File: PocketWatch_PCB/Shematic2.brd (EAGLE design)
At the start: 45 x 25 mm, 53 parts, among them IC1 74HC139D, Q1 BCX71SMD, Q2 BCX71SMD, Q3 BCX71SMD, Q4 BCX71SMD, U2 ATTINY88-AU

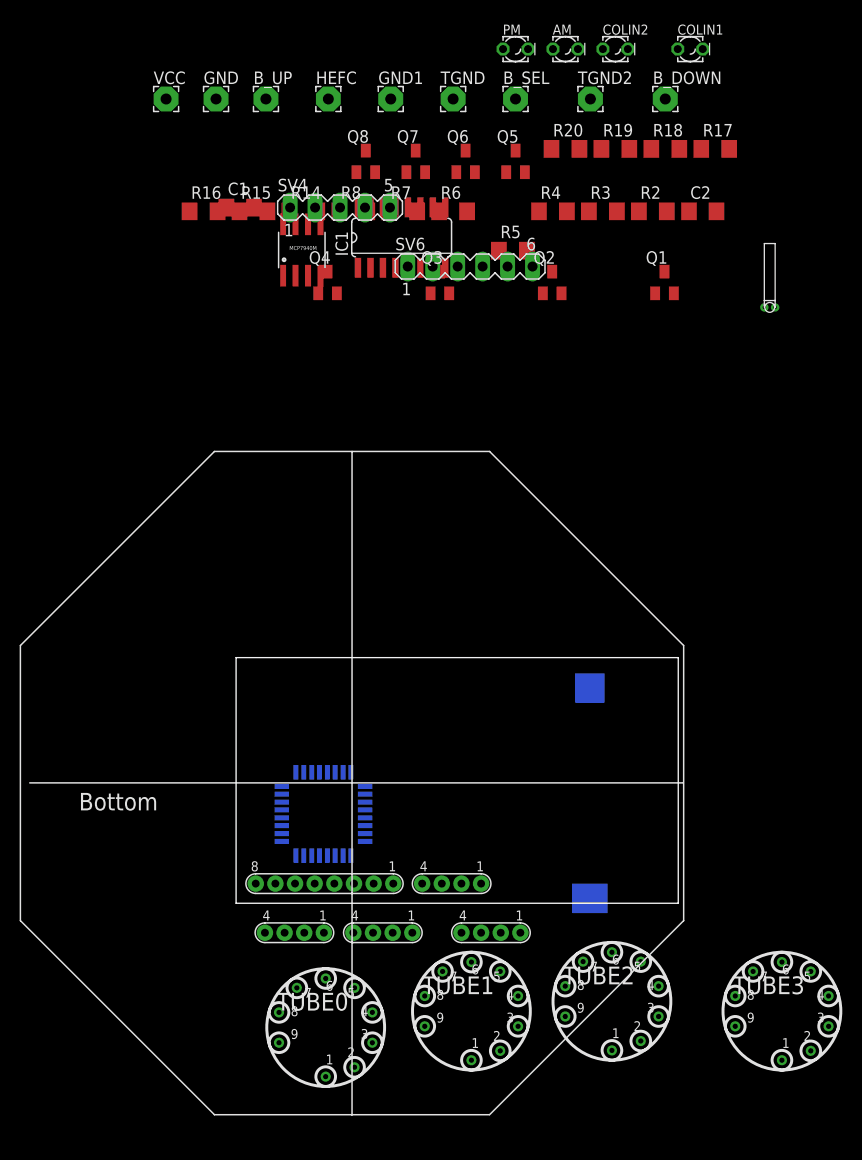
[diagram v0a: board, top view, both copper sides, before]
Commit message: Schematic updates. Began component layout.
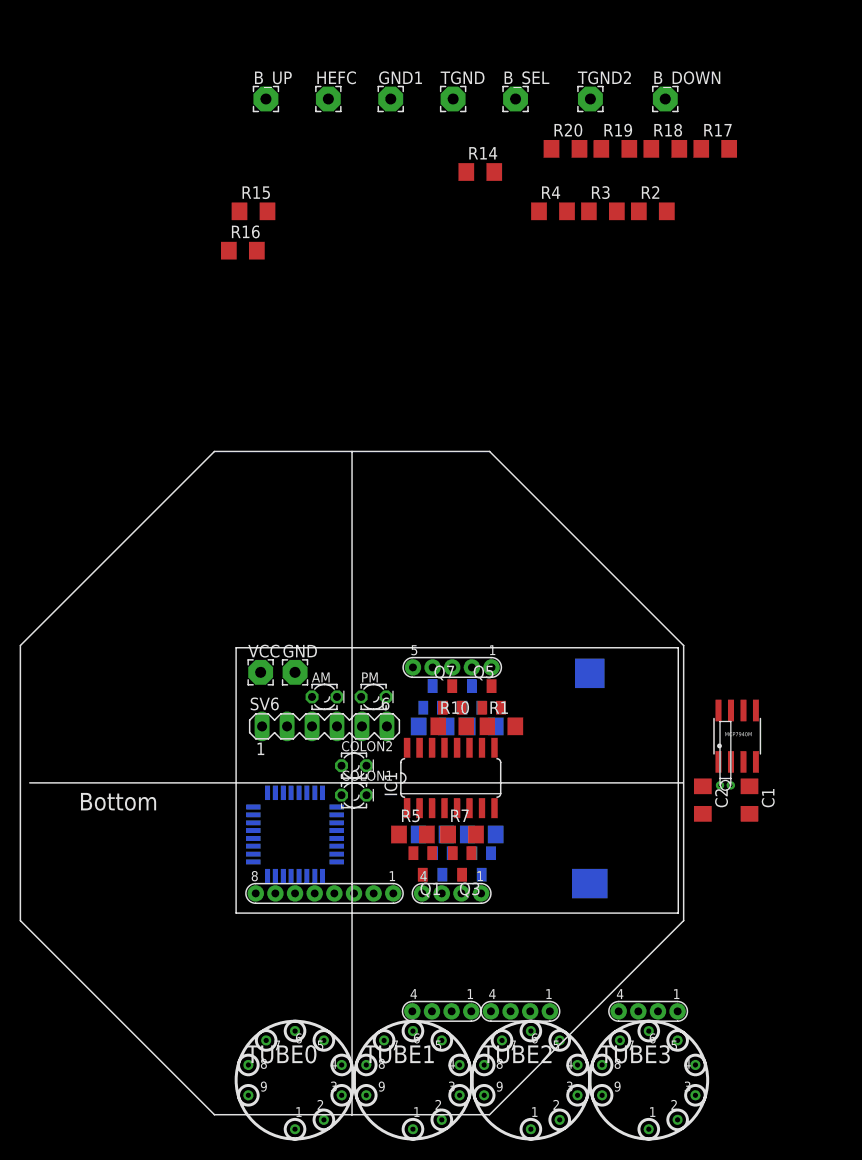
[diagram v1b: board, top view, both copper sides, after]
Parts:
- removed COLIN1, COLIN2: (no value), eagle-ltspice:LED_LD260
- added COLON1, COLON2: (no value), eagle-ltspice:LED_LD260
- added R1, R10, R11, R9: 1k, eagle-ltspice:R1206
- SV4: value (none) -> H05; device con-lstb:MA05-1 -> Library:H05
- moved C1 79.5 mm to (63.2, 33.5), turned to 270 degrees
- moved AM 70.3 mm to (20.0, 44.0)
- moved PM 67.5 mm to (25.0, 44.0)
- moved MCP7940M 66.4 mm to (62.0, 40.0)
- moved R8 64.8 mm to (36.0, 30.0), flipped to the bottom
- moved Q1 64.1 mm to (30.0, 27.0), turned to 180 degrees
- moved R7 63.7 mm to (34.0, 30.0)
- moved R6 63.5 mm to (31.0, 30.0), flipped to the bottom
- moved Q4 61.2 mm to (36.0, 27.0), flipped to the bottom, turned to 180 degrees
- moved R5 60.3 mm to (29.0, 30.0)
- moved Q2 60.2 mm to (32.0, 27.0), flipped to the bottom, turned to 180 degrees
- moved C2 59.9 mm to (58.5, 33.5), turned to 270 degrees
- moved Q3 59.2 mm to (34.0, 27.0), turned to 180 degrees
- moved VCC 59.1 mm to (13.5, 46.5)
- moved GND 58.9 mm to (17.0, 46.5)
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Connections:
- new net N$23: Q5.1, R1.1
- new net N$24: Q6.1, R9.1
- new net N$25: Q7.1, R10.1
- new net N$26: Q8.1, R11.1
- net M0: now also R1.2; no longer Q5.1
- net M1: now also R9.2; no longer Q6.1
- net M2: now also R10.2; no longer Q7.1
- net M3: now also R11.2; no longer Q8.1
- net N$7: now also COLON1.A; no longer COLIN1.A
- net N$9: now also COLON2.A; no longer COLIN2.A
- net VCC: now also COLON1.K, COLON2.K; no longer COLIN1.K, COLIN2.K
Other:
- board size 45 x 25 mm -> 45 x 27 mm

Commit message: File Update
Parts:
- moved R14 67.3 mm to (20.0, 32.0), turned to 270 degrees
- moved R17 65.3 mm to (20.0, 48.0)
- moved R15 56.9 mm to (20.0, 37.0), turned to 90 degrees
- moved R16 43.5 mm to (25.0, 48.0), turned to 180 degrees
- moved R2 42.4 mm to (55.0, 51.0), turned to 180 degrees
- moved R3 40.0 mm to (55.0, 54.0), turned to 180 degrees
- moved R4 38.3 mm to (55.0, 57.0), turned to 180 degrees
- moved R19 35.1 mm to (14.6, 101.8)
- moved U$5 18.0 mm to (48.0, 44.5), turned to 180 degrees
- moved C1 13.2 mm to (50.0, 33.5)
- moved R18 13.2 mm to (41.7, 101.8)
- moved MCP7940M 13.0 mm to (49.0, 40.0)
- moved C2 12.8 mm to (45.8, 33.5)
- moved 6PF 11.8 mm to (48.5, 35.0), turned to 180 degrees
- moved R20 11.2 mm to (55.5, 101.8)
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
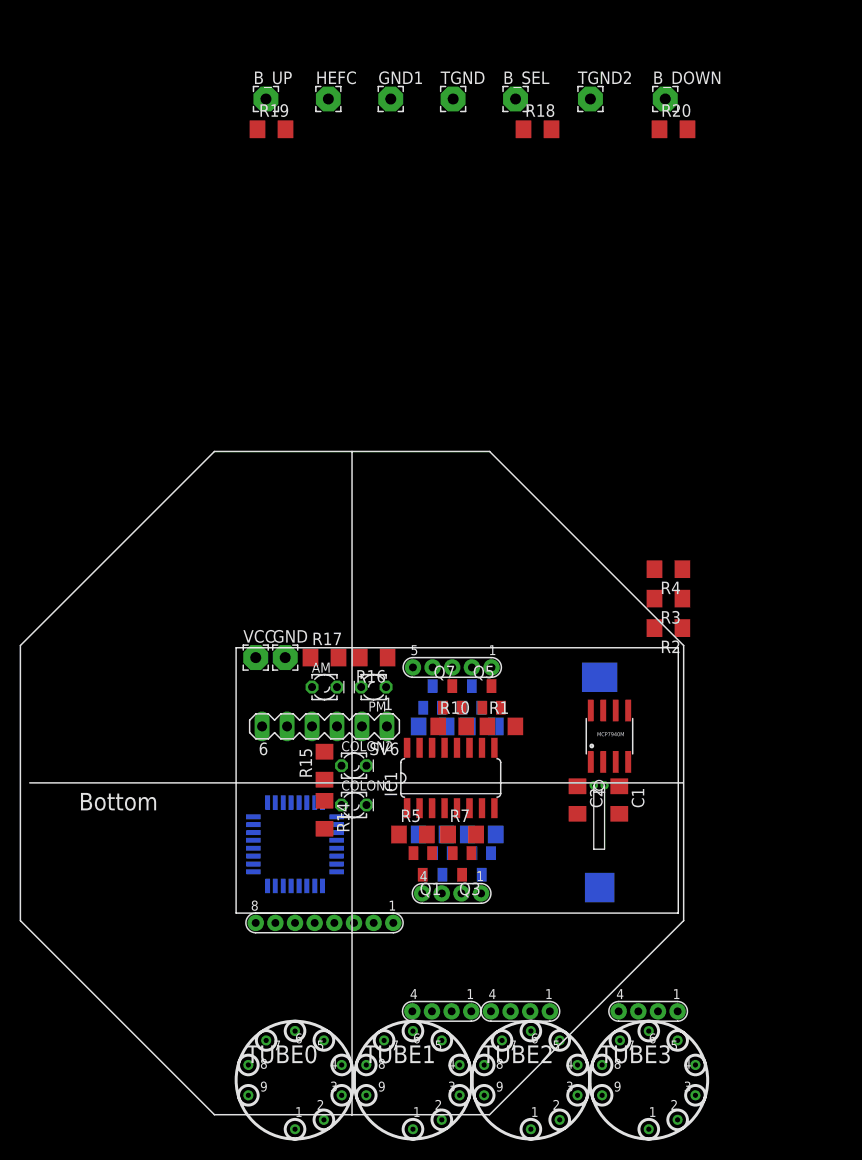
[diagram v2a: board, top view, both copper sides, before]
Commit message: Swapped to using stepper motor driver. Routed board
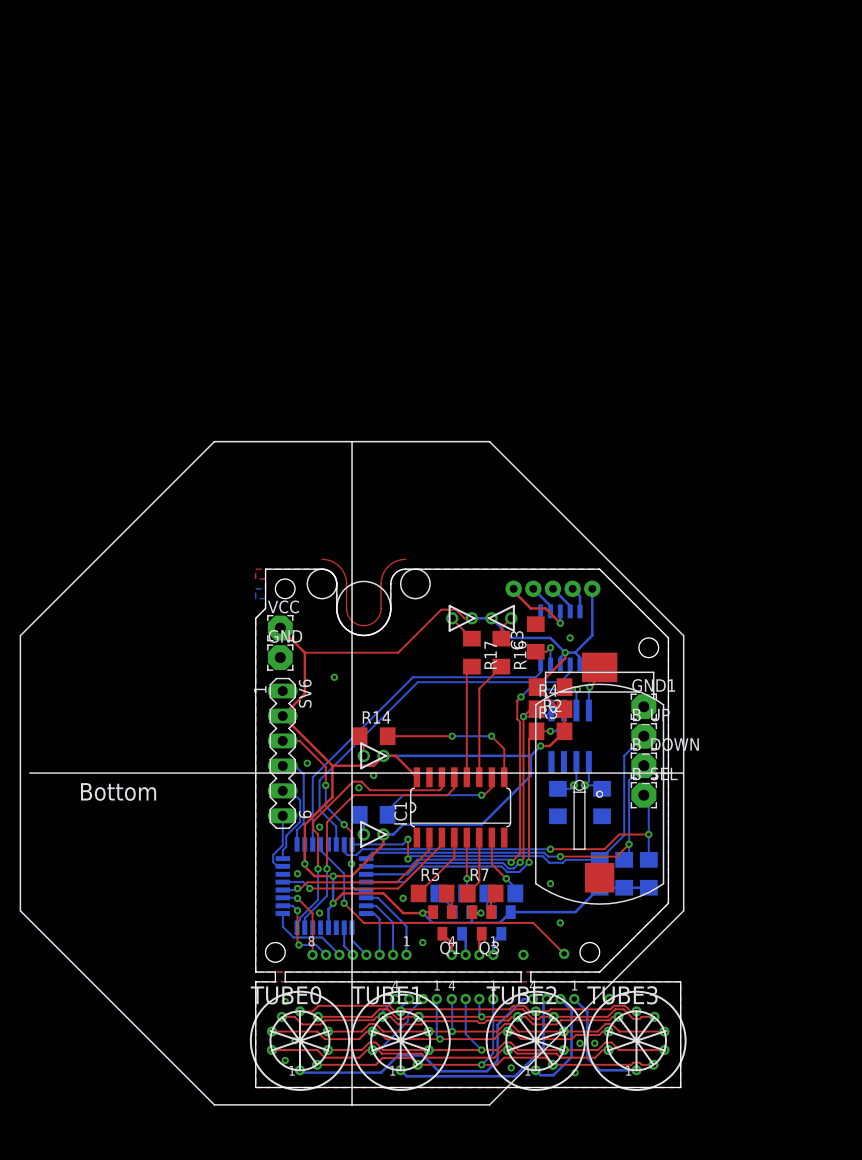
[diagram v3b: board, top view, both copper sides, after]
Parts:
- removed COLON1, COLON2: (no value), eagle-ltspice:LED_LD260
- removed Q5, Q6, Q7, Q8: (no value), transistor-npn:SOT23
- removed R1, R10, R11, R9: 1k, eagle-ltspice:R1206
- added C3: 0.01uF, eagle-ltspice:C1206
- added COLIN1, COLIN2: LED, Library:LED
- added U$1: LB1848MC, Library:LB1848MC
- AM, PM: value (none) -> LED; device eagle-ltspice:LED_LD260 -> Library:LED
- HEFC: value (none) -> H01; device wirepad:2,54/1,1 -> Library:H01
- TGND, TGND2: value WIREPAD2,54/1,1 -> H01; device wirepad:2,54/1,1 -> Library:H01
- moved TGND 93.0 mm to (49.0, 13.2)
- moved HEFC 90.2 mm to (44.4, 17.9)
- moved TGND2 87.4 mm to (40.2, 17.8)
- moved R19 82.8 mm to (48.0, 26.0), flipped to the bottom, turned to 270 degrees
- moved R18 76.6 mm to (53.0, 26.0), flipped to the bottom, turned to 270 degrees
- moved R20 75.9 mm to (50.5, 26.0), flipped to the bottom, turned to 270 degrees
- moved B_UP 75.4 mm to (52.5, 40.0)
- moved B_SEL 72.0 mm to (52.5, 34.0)
- moved B_DOWN 67.9 mm to (52.5, 37.0)
- moved GND1 67.0 mm to (52.5, 43.0)
- moved R4 18.6 mm to (43.0, 42.8), turned to 0 degrees
- moved R3 18.1 mm to (43.0, 40.5), turned to 0 degrees
- moved AM 15.7 mm to (34.0, 52.0)
- moved R17 15.0 mm to (35.0, 48.5), turned to 270 degrees
- moved PM 14.8 mm to (38.0, 52.0)
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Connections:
- removed net M2: R10.2, U2.3
- removed net M3: R11.2, U2.6
- removed net N$23: Q5.1, R1.1
- removed net N$24: Q6.1, R9.1
- removed net N$25: Q7.1, R10.1
- removed net N$26: Q8.1, R11.1
- new net N$31: C3.1, U$1.SOF
- net GND: now also C3.2, TGND2.P$1, U$1.GND; no longer Q5.2, Q6.2, Q7.2, Q8.2, TGND2.1
- net HEF: now also HEFC.P$1; no longer HEFC.1
- net M0: now also U$1.IN1; no longer R1.2
- net M1: now also U$1.IN2; no longer R9.2
- net N$12: now also PM.P$1; no longer PM.A
- net N$14: now also AM.P$1; no longer AM.A
- net N$19: now also SV4.4, U$1.OUT4; no longer Q5.3, SV4.1
- net N$20: now also SV4.3, U$1.OUT3; no longer Q6.3, SV4.2
- net N$21: now also SV4.2, U$1.OUT2; no longer Q7.3, SV4.3
- net N$22: now also SV4.1, U$1.OUT1; no longer Q8.3, SV4.4
- net N$7: now also COLIN1.P$1; no longer COLON1.A
- net N$9: now also COLIN2.P$1; no longer COLON2.A
- net TGND: now also TGND.P$1; no longer TGND.1
- net VCC: now also AM.P$2, COLIN1.P$2, COLIN2.P$2, PM.P$2, U$1.ENA, U$1.VCC; no longer AM.K, COLON1.K, COLON2.K, PM.K
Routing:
- net VCC: track 0.00 -> 187.7 mm, vias 0 -> 7
- net SEG_E_2: track 0.00 -> 43.9 mm
- net B_UP: track 0.00 -> 43.0 mm, vias 0 -> 2
- net SEG_DOT_2: track 0.00 -> 42.8 mm, vias 0 -> 1
- net MFP: track 0.00 -> 42.3 mm, vias 0 -> 3
- net SEG_B_2: track 0.00 -> 42.0 mm, vias 0 -> 1
- net SEG_D_2: track 0.00 -> 40.4 mm, vias 0 -> 1
- net B_SEL: track 0.00 -> 39.5 mm, vias 0 -> 2
- net SEG_C_2: track 0.00 -> 39.5 mm, vias 0 -> 1
- net SEG_G_2: track 0.00 -> 38.7 mm
- net SEG_A_2: track 0.00 -> 38.6 mm, vias 0 -> 1
- net B_DOWN: track 0.00 -> 38.1 mm, vias 0 -> 2
- net M1: track 0.00 -> 38.1 mm
- net SEG_F_2: track 0.00 -> 37.3 mm
- net SDA: track 0.00 -> 36.3 mm, vias 0 -> 2
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- added copper zone on layer 1, net GND
- added copper zone on layer 16, net GND
- added copper zone on layer 1, net TGND
- added copper zone on layer 16, net TGND
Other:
- board size 45 x 27 mm -> 43.2 x 52.8 mm

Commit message: File Upload
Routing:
- net N$23: track 15.6 -> 0.00 mm
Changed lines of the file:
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@@
 <via x="39" y="6.25" extent="1-16" drill="0.35"/>
-</signal>
-<signal name="N$23">
-<wire x1="25.75" y1="55.5" x2="28.25" y2="58" width="0" layer="1" curve="-90"/>
-<wire x1="19.75" y1="58" x2="22.25" y2="55.5" width="0" layer="1" curve="-90"/>
-<wire x1="25.75" y1="53" x2="25.75" y2="55.5" width="0" layer="1"/>
-<wire x1="25.75" y1="53" x2="22.25" y2="53" width="0" layer="1" curve="-180"/>
-<wire x1="22.25" y1="53" x2="22.25" y2="55.5" width="0" layer="1"/>
 </signal>
 </signals>

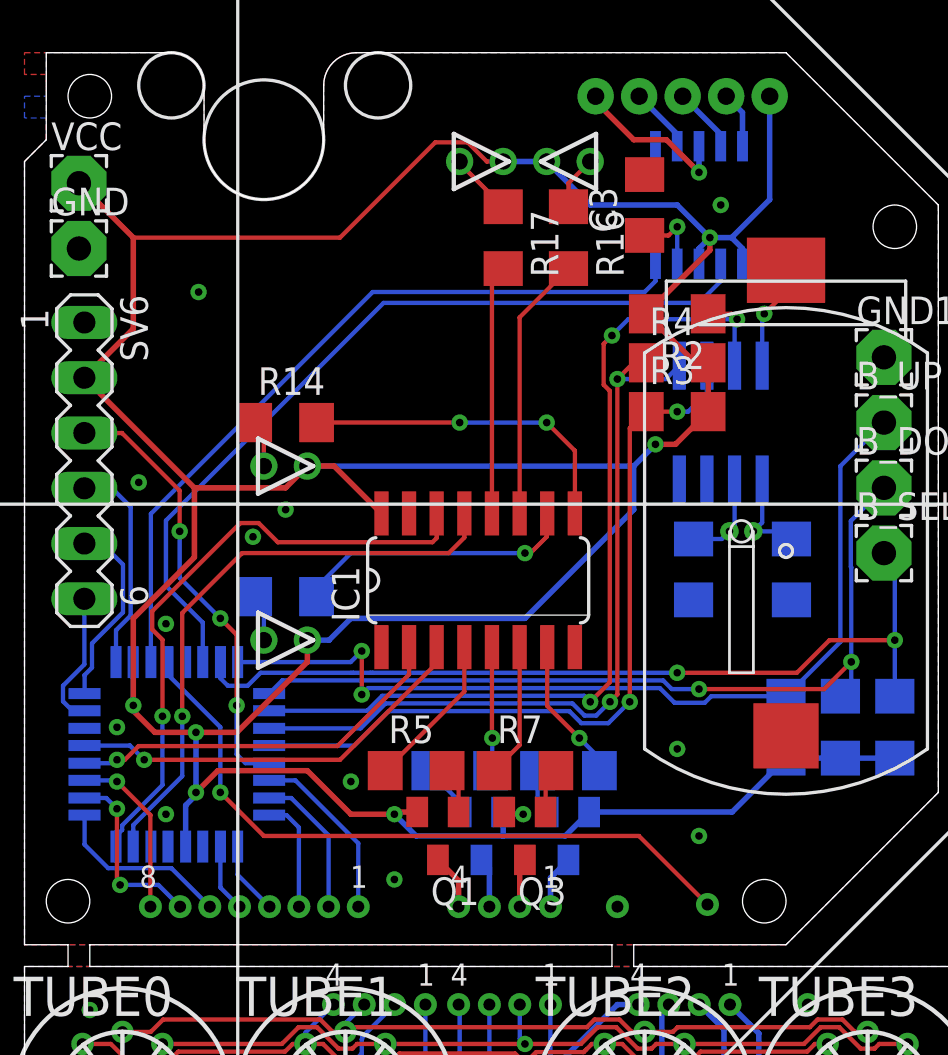
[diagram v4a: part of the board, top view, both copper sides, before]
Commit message: Added bypass capacitors. Revised routing.
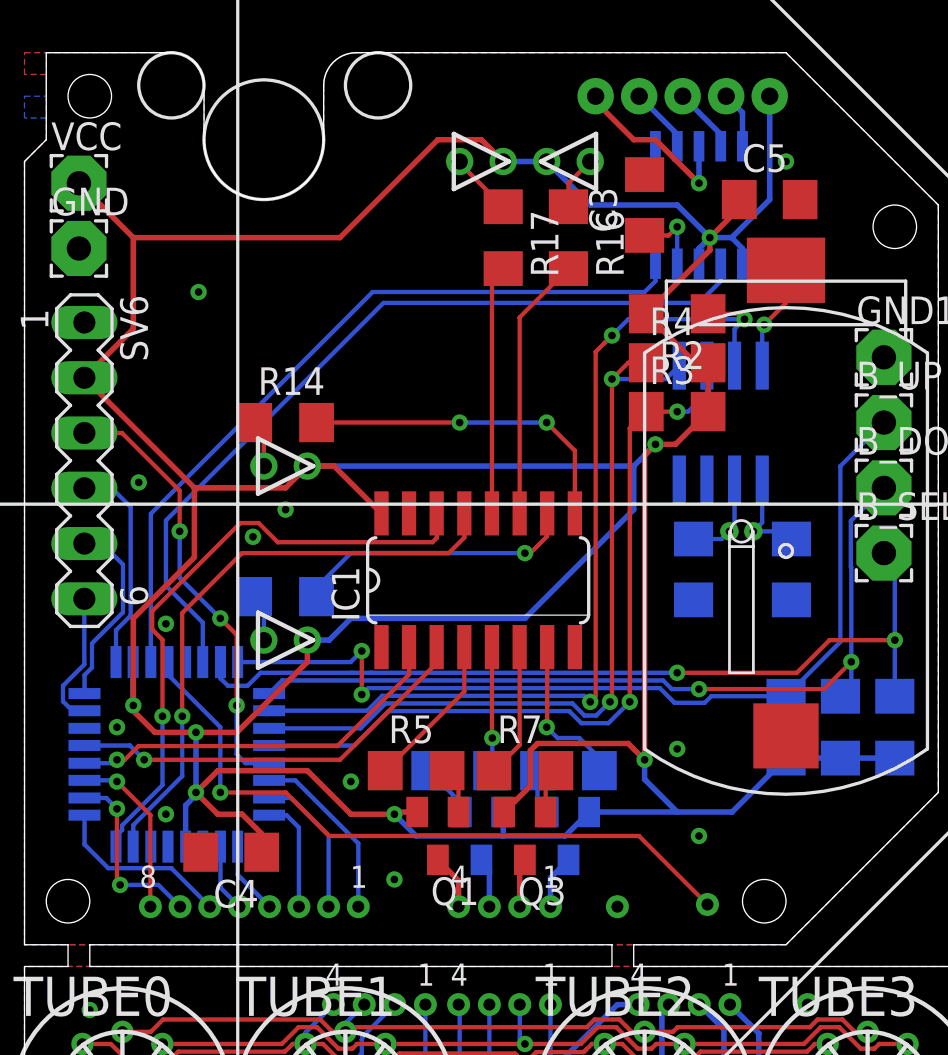
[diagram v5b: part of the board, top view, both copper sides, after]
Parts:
- added C4, C5: 10uF, eagle-ltspice:C1206
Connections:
- net GND: now also C4.2, C5.2
- net VCC: now also C4.1, C5.1
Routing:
- net VCC: track 187.7 -> 219.8 mm
- net MFP: track 42.3 -> 43.4 mm
- net SDA: track 36.3 -> 37.3 mm
- net N$22: track 7.55 -> 8.25 mm
- net N$13: track 6.67 -> 7.28 mm
